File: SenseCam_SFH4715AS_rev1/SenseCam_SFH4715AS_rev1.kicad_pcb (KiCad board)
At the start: 2 copper layers, 65 x 26 mm, 16 parts, among them J1 Conn_01x03, J2 Conn_01x03, P1 CA16372_HB-SQ-WWW, P2 CA16372_HB-SQ-WWW

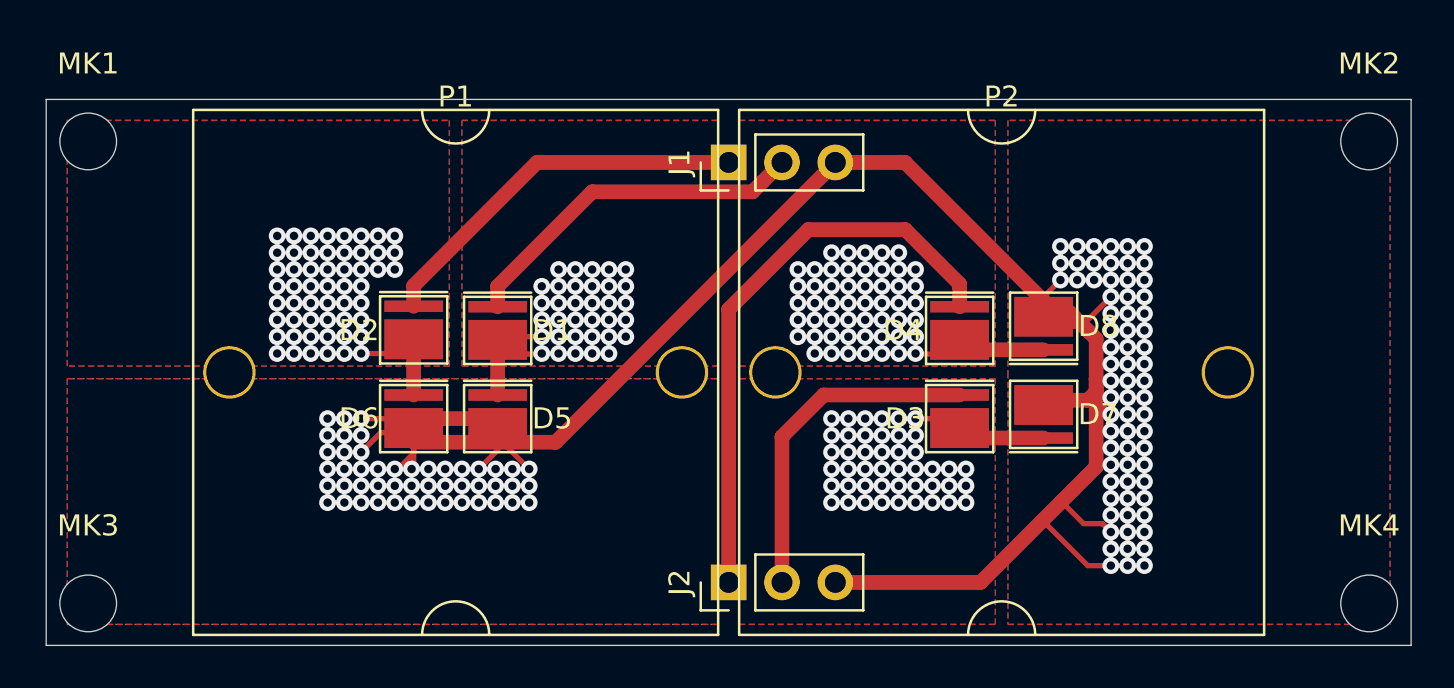
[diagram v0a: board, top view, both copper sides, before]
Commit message: Add silkscreen stuff and fix a copper pour
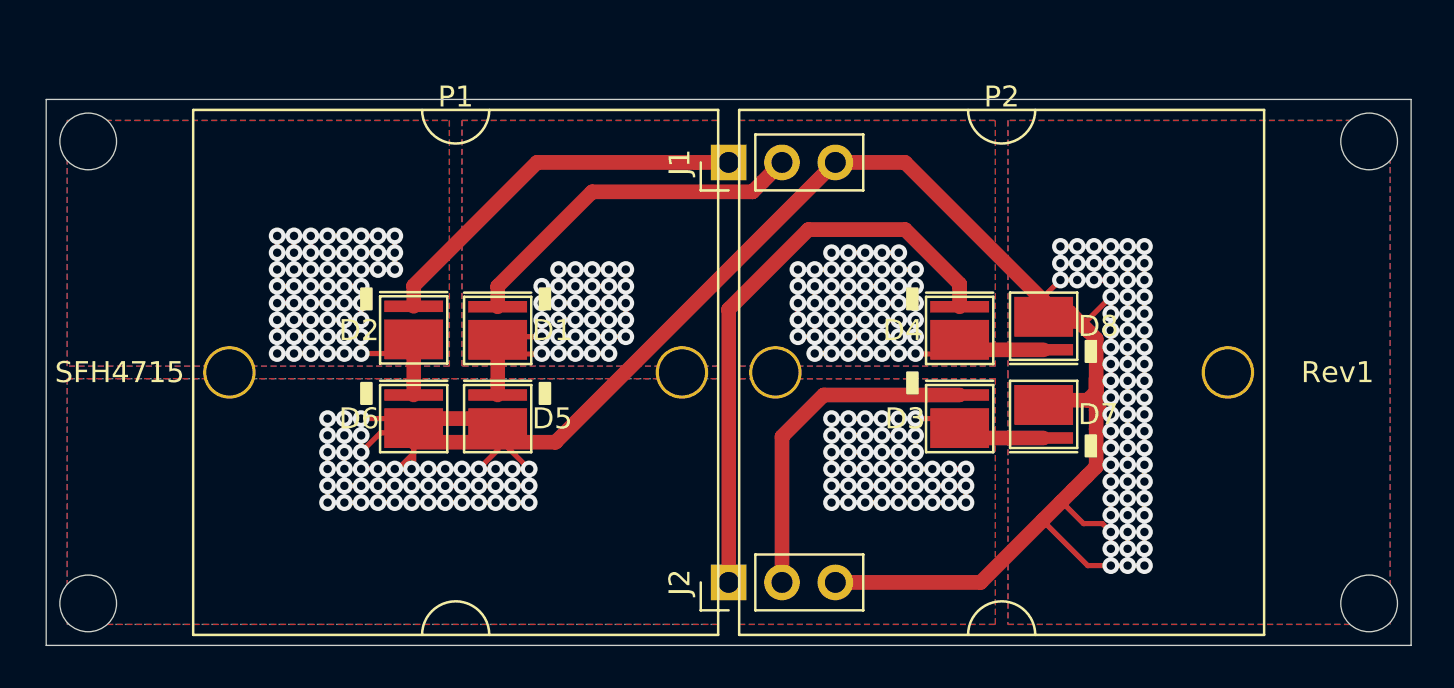
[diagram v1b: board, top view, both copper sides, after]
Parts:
- added G***: Appiko_Logo_2, sense_fp:Appiko_Logo_2, B.Cu at (65.0, 14.0)
- added G***: Appiko_LOGO_img, sense_fp:Appiko_LOGO_img, B.Cu at (18.0, 18.0)
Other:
- board text added: "Rev1"
- board text added: "SFH4715"
